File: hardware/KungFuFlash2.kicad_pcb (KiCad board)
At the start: 2 copper layers, 60.6 x 62 mm, 57 parts, among them J1 DNP, J2 USB_C_Receptacle_USB2.0, J3 DNP, Q1 BC817-40, SW1 ES411X-10XX-43X-16-B, SW2 ES411X-10XX-43X-16-B, SW3 ES411X-10XX-43X-16-B, U1 Edge Connector, Immersion gol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, U2 AMS1117-3.3, U3 STM32H7B0VBTx, Y1 25 MHz

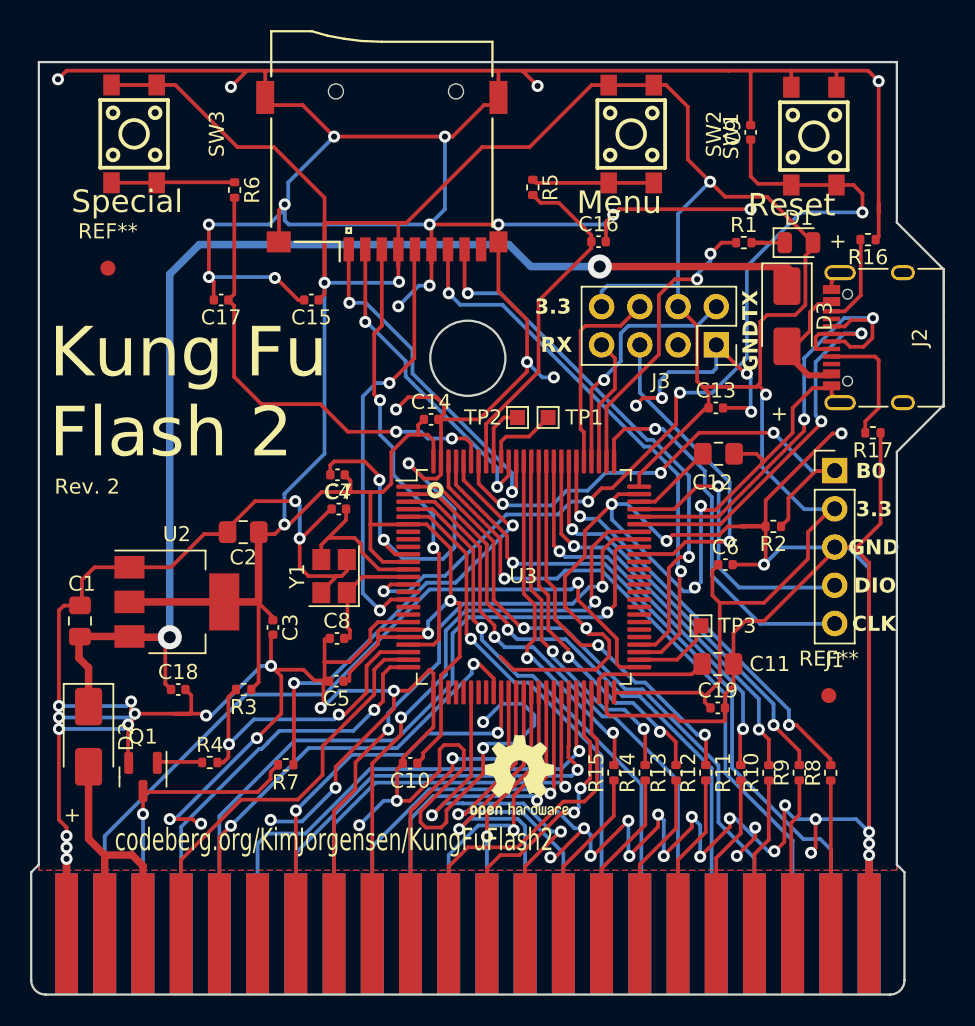
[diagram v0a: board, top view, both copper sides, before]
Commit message: Add constrained 1x2 PCB panelization
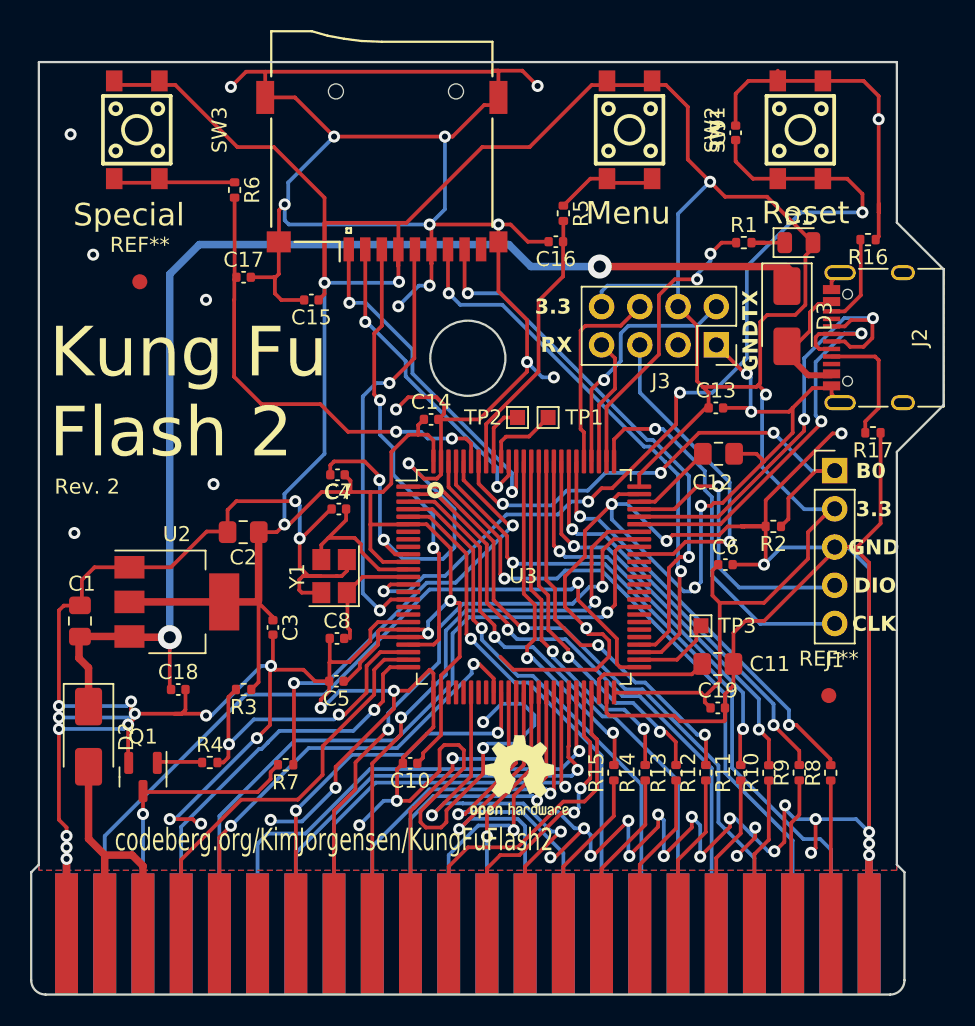
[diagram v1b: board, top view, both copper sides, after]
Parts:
- moved C16 2.84 mm to (110.8, 80.1), turned to 180 degrees
- moved R5 2.66 mm to (111.2, 78.2)
- moved REF** 2.30 mm to (83.1, 82.8)
- moved C17 2.13 mm to (90.0, 82.5), turned to 0 degrees
- moved C9 1.00 mm to (122.7, 72.9)
- moved SW1 0.99 mm to (127.0, 72.7)
- moved SW3 0.32 mm to (82.9, 72.7)
- moved SW2 0.30 mm to (115.7, 72.7)
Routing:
- net GND: track 659.1 -> 599.2 mm, vias 76 -> 73
- net /MENU: track 22.9 -> 18.1 mm
- net Net-(R5-Pad1): track 8.13 -> 6.97 mm
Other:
- board text removed: "+"
